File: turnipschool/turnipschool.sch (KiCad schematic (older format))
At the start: 59 parts, among them J1 USB-DEVICE-SHIELD, P1 CONN_1, P2 RESET_N, P3 DD, P4 DC, P5 3V3, P6 GND, P7 CABLE, T1 BALUN, U1 CC1111, U2 AP7313, U3 USB2412, U4 AP2511SN-7, X1 GSG-XTAL4PIN, X2 GSG-XTAL4PIN

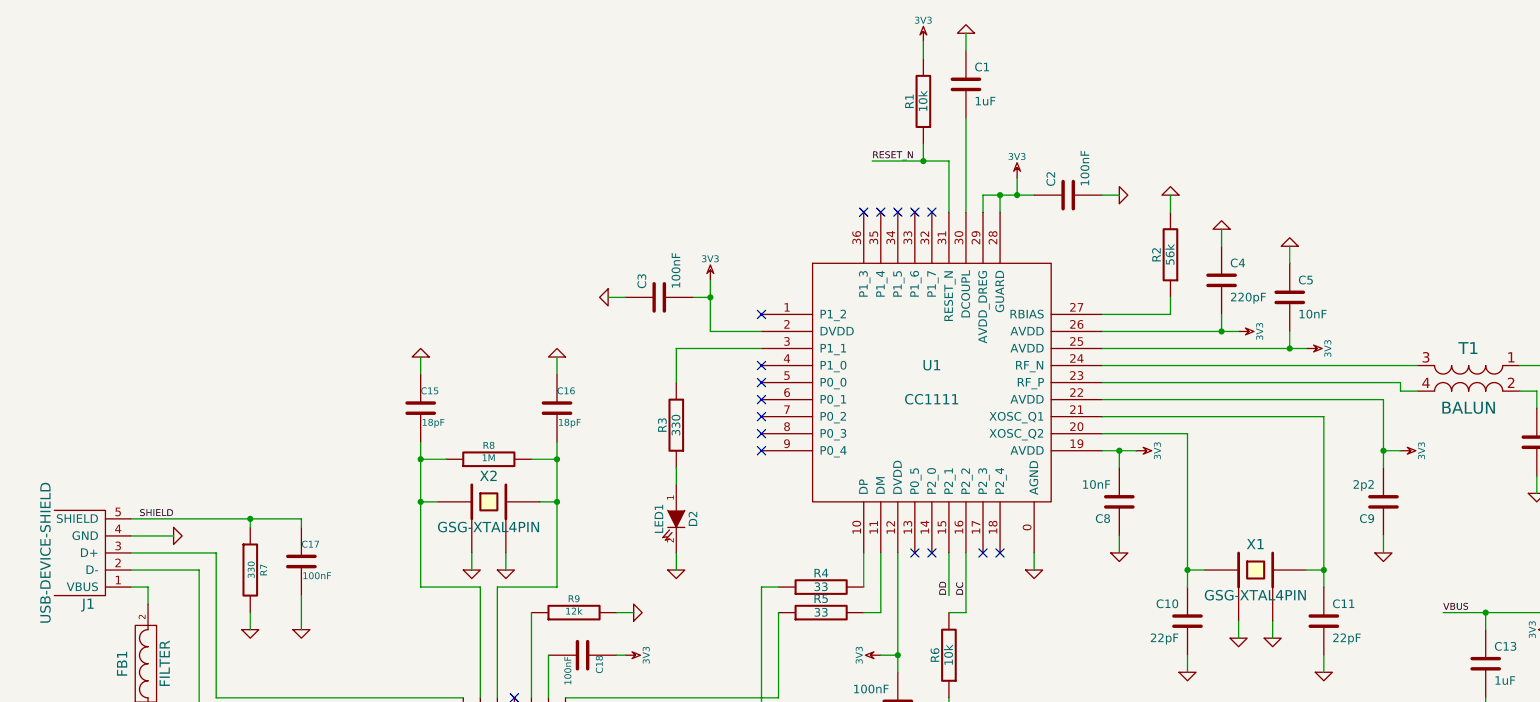
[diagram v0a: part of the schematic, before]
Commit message: magnetic sensor for bootloader activation
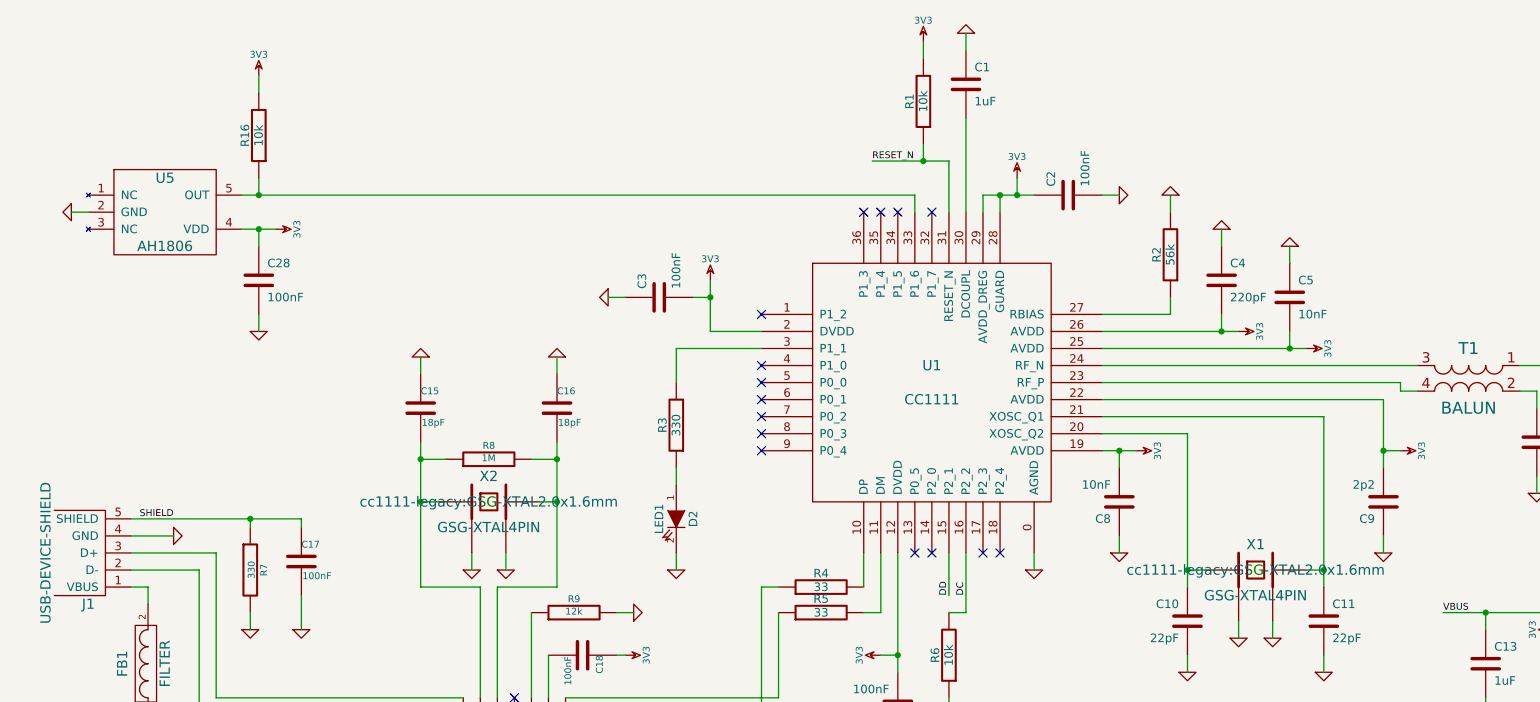
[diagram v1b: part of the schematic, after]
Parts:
- added C28: 100nF, cc1111-legacy:GSG-0402, symbol C
- added R16: 10k, cc1111-legacy:GSG-0402, symbol R
- added U5: AH1806, cc1111-legacy:GSG-SOT553, symbol AH180N-ZG
- C1, C10, C11, C12, C13, C14, C15, C16, C17, C18, C19, C2, C20, C21, C22, C23, C24, C25, C26, C3, C4, C5, C6, C7, C8, C9, R1, R10, R11, R12, R13, R14, R15, R2, R3, R4, R5, R6, R7, R8, R9: footprint (none) -> cc1111-legacy:GSG-0402
- C27, FB1: footprint (none) -> cc1111-legacy:GSG-0805
- D2: footprint (none) -> cc1111-legacy:GSG-0603D
- J1: footprint (none) -> cc1111-legacy:GSG-USB-A-1001-010-01001-SHIELD
- P1: footprint (none) -> cc1111-legacy:GSG-50MIL-HEADER-1x1-TH
- P2, P3, P4, P5, P6: footprint (none) -> cc1111-legacy:GSG-TESTPOINT-50MIL
- P7: footprint (none) -> cc1111-legacy:GSG-50MIL-HEADER-1x5-TH
- T1: footprint (none) -> cc1111-legacy:GSG-B0310J50100AHF
- U1: footprint (none) -> cc1111-legacy:GSG-QFN36
- U2: footprint (none) -> cc1111-legacy:GSG-SOT23-3
- U3: footprint (none) -> cc1111-legacy:GSG-QFN28
- U4: footprint (none) -> cc1111-legacy:GSG-U-DFN2020-6
- X1, X2: footprint ~ -> cc1111-legacy:GSG-XTAL2.0x1.6mm
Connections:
- net 3V3: now also C28.1, R16.2, U5.4 (VDD)
- net GND: now also C28.2, U5.2 (GND)
- net at U1.33 (P1_6): now also R16.1, U5.5 (OUT)
- no-connect marks 23 -> 22

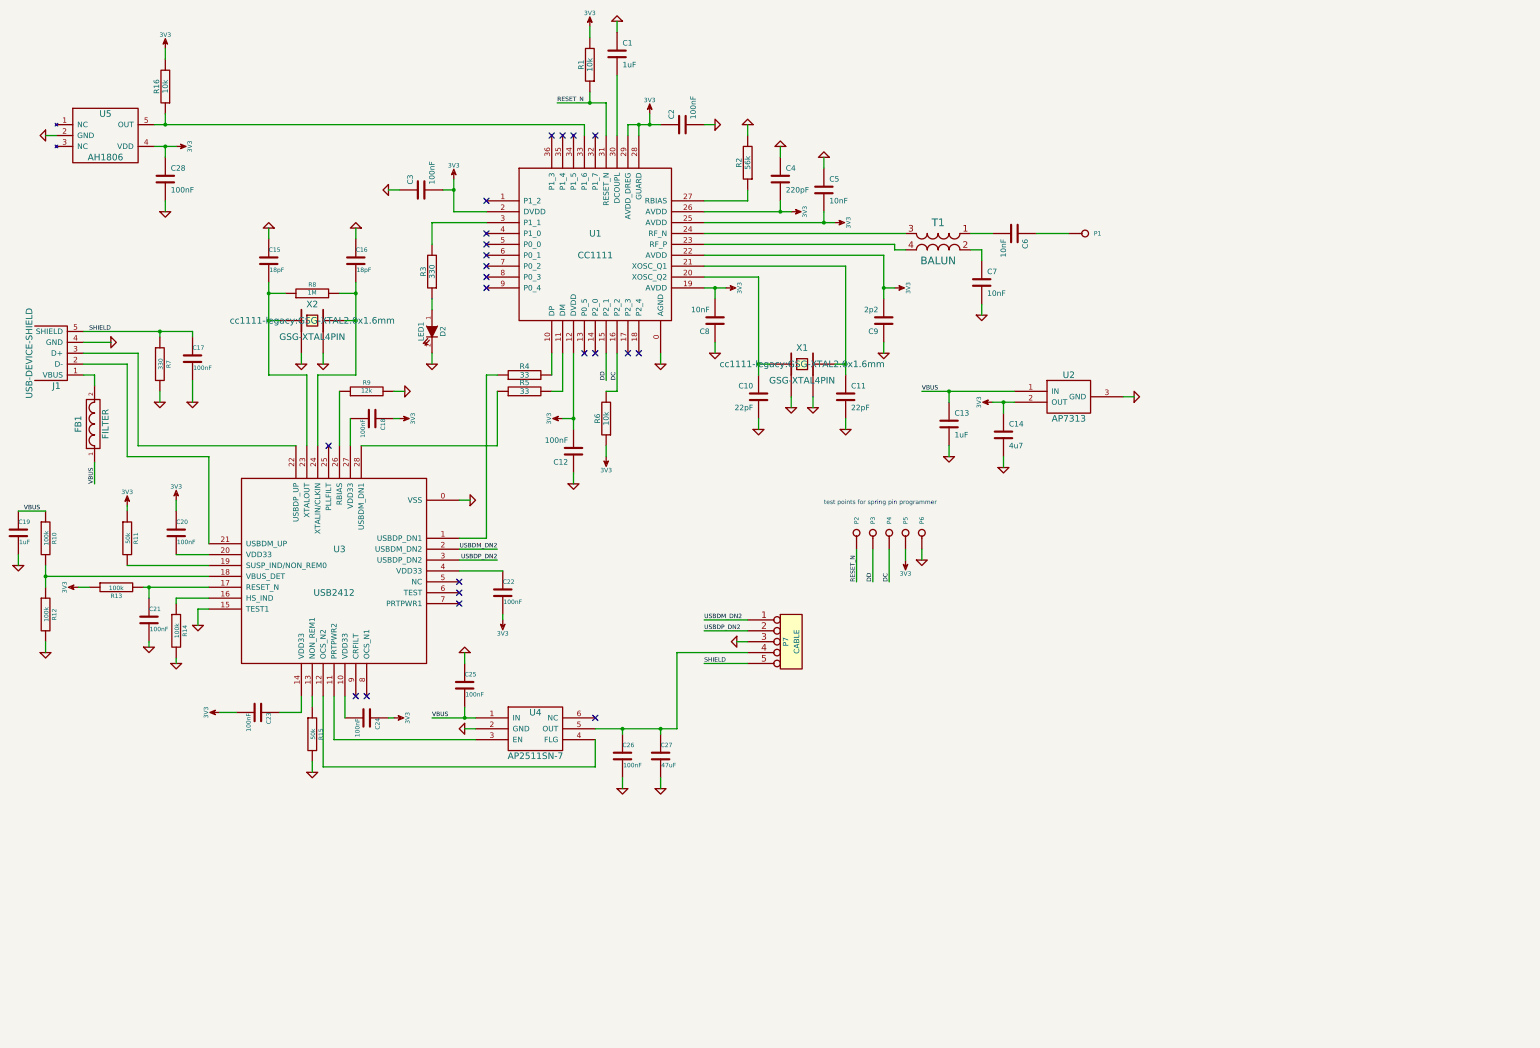
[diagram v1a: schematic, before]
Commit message: corrected hub supply connections, added required 1.5k USB pull-up, removed debug LED
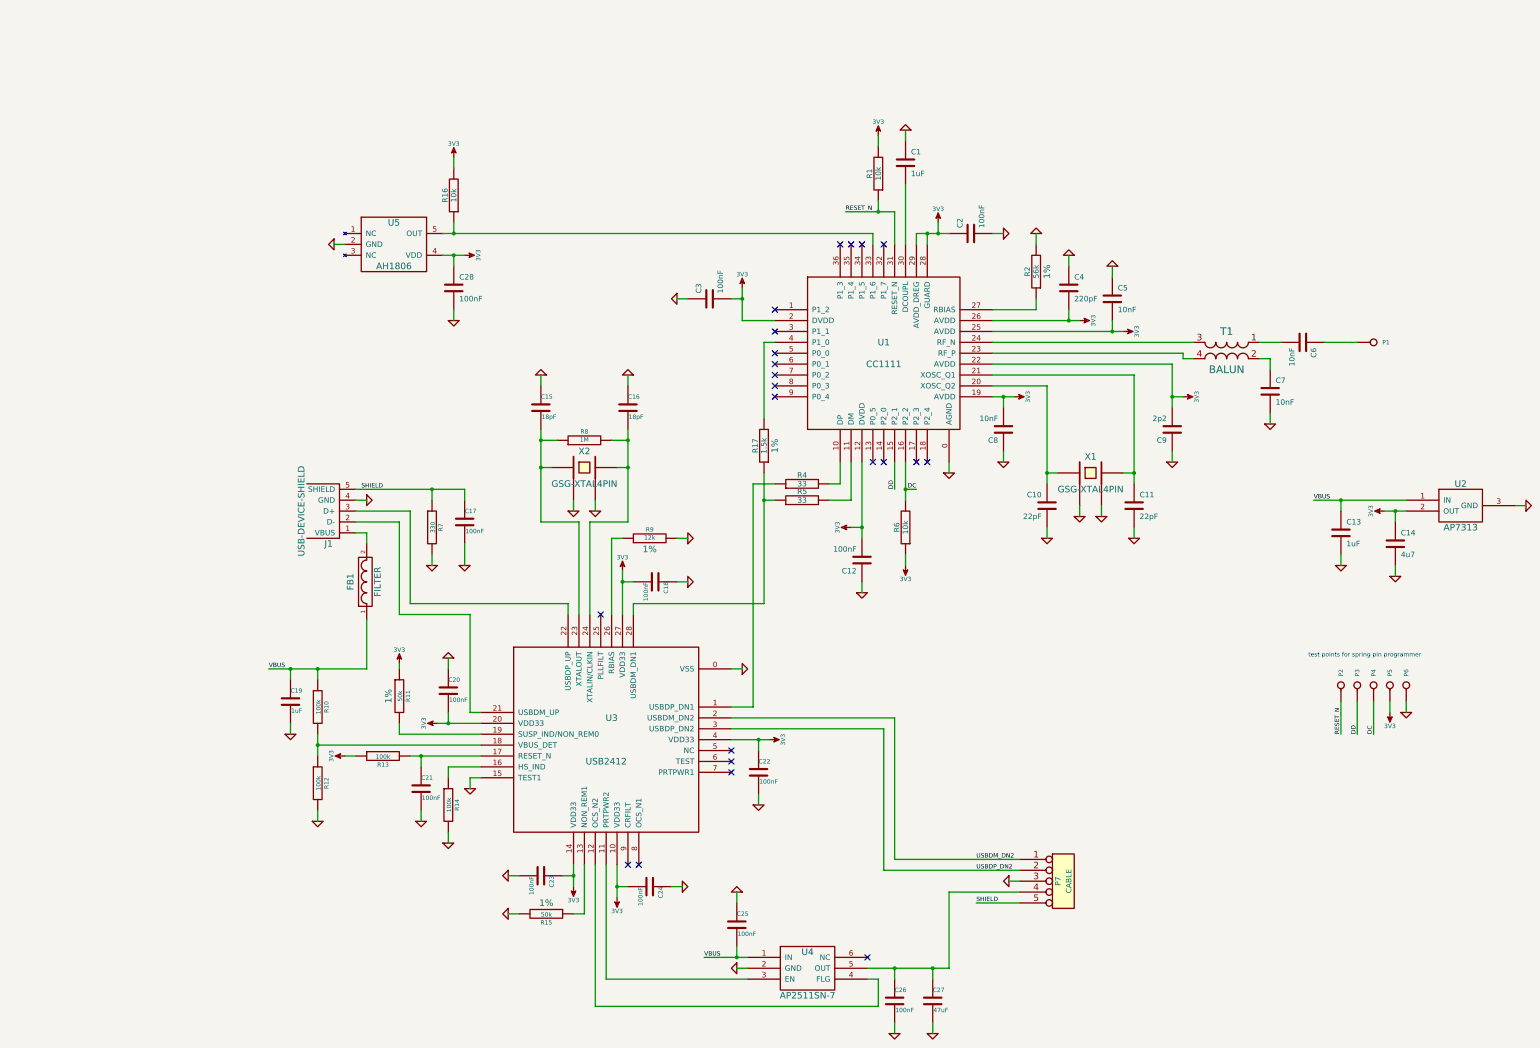
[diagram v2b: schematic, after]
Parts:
- removed D2: LED1, cc1111-legacy:GSG-0603D, symbol LED
- removed R3: 330, cc1111-legacy:GSG-0402, symbol R
- added R17: 1.5k, cc1111-legacy:GSG-0402, symbol R
- R11, R15, R2, R9: Note (none) -> 1%
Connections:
- net 3V3: now also C18.2, C20.2, C22.1, C23.1, C24.2, U3.10 (VDD33), U3.14 (VDD33), U3.20 (VDD33), U3.27 (VDD33), U3.4 (VDD33); no longer C18.1, C20.1, C22.2, C23.2, C24.1
- net GND: now also C18.1, C20.1, C22.2, C23.2, C24.1
- net at R5.1, U3.28 (USBDM_DN1): now also R17.1
- net at U1.4 (P1_0): now also R17.2
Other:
- moved on the sheet: C1, C10, C11, C12, C13, C14, C15, C16, C17, C18, C19, C2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

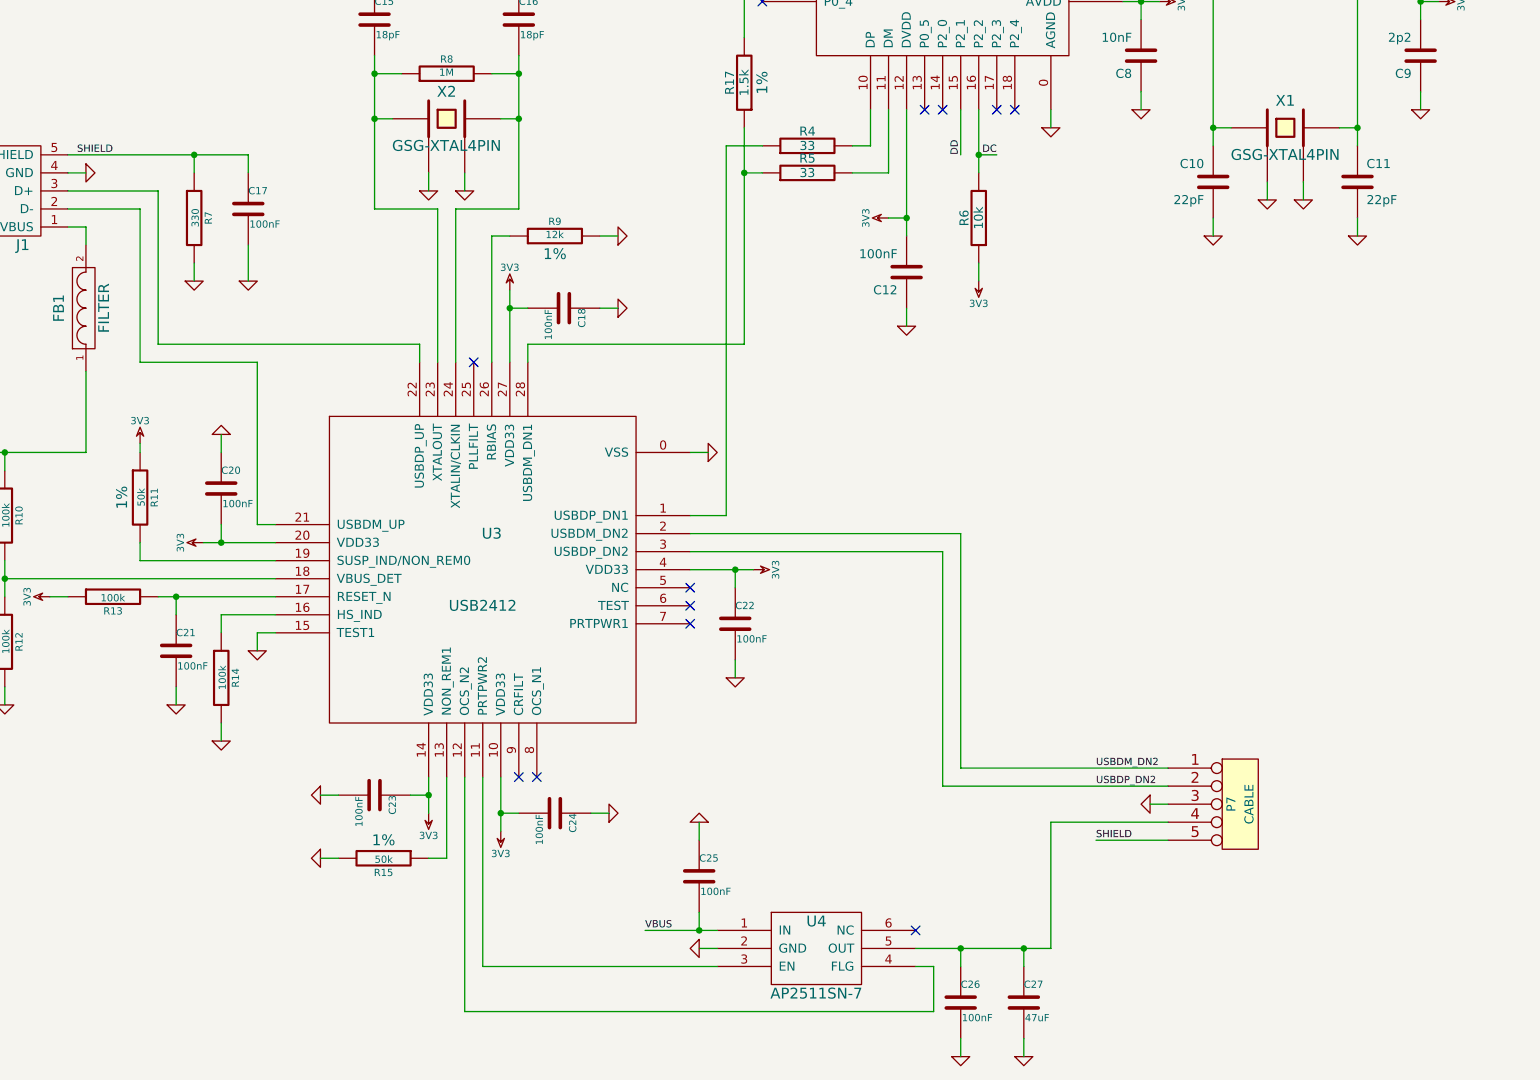
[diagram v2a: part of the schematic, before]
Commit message: swapped downstream USB ports, made CC1111 port removable on the hub, improved layout
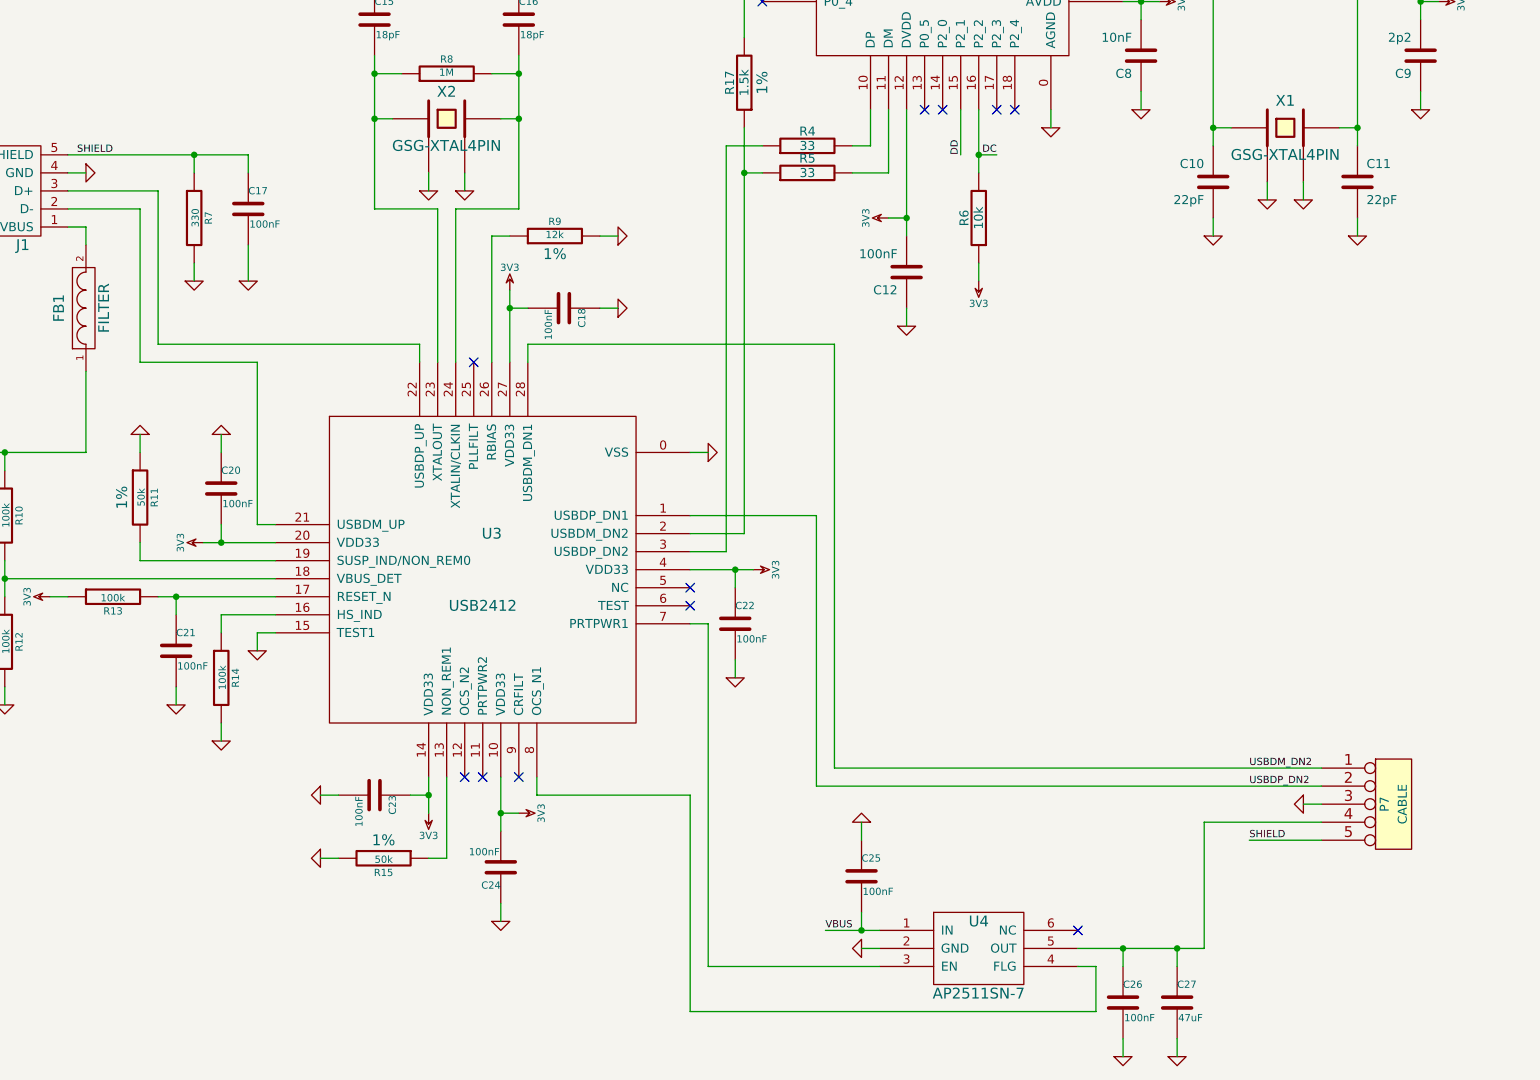
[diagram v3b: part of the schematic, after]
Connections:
- net 3V3: no longer R11.1
- net GND: now also R11.1
- net USBDM_DN2: now also U3.28 (USBDM_DN1); no longer U3.2 (USBDM_DN2)
- net USBDP_DN2: now also U3.1 (USBDP_DN1); no longer U3.3 (USBDP_DN2)
- net at R4.1: now also U3.3 (USBDP_DN2); no longer U3.1 (USBDP_DN1)
- net at R17.1, R5.1: now also U3.2 (USBDM_DN2); no longer U3.28 (USBDM_DN1)
- net at U3.11 (PRTPWR2): no longer U4.3 (EN)
- net at U3.12 (OCS_N2): no longer U4.4 (FLG)
- net at U3.7 (PRTPWR1): now also U4.3 (EN)
- net at U3.8 (OCS_N1): now also U4.4 (FLG)
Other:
- moved on the sheet: C24, C25, C26, C27, P7, U4
